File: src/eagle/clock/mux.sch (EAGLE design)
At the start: 53 parts, among them U1 SN74HC595N, U2 SN74HC595N, U3 SN74HC595N

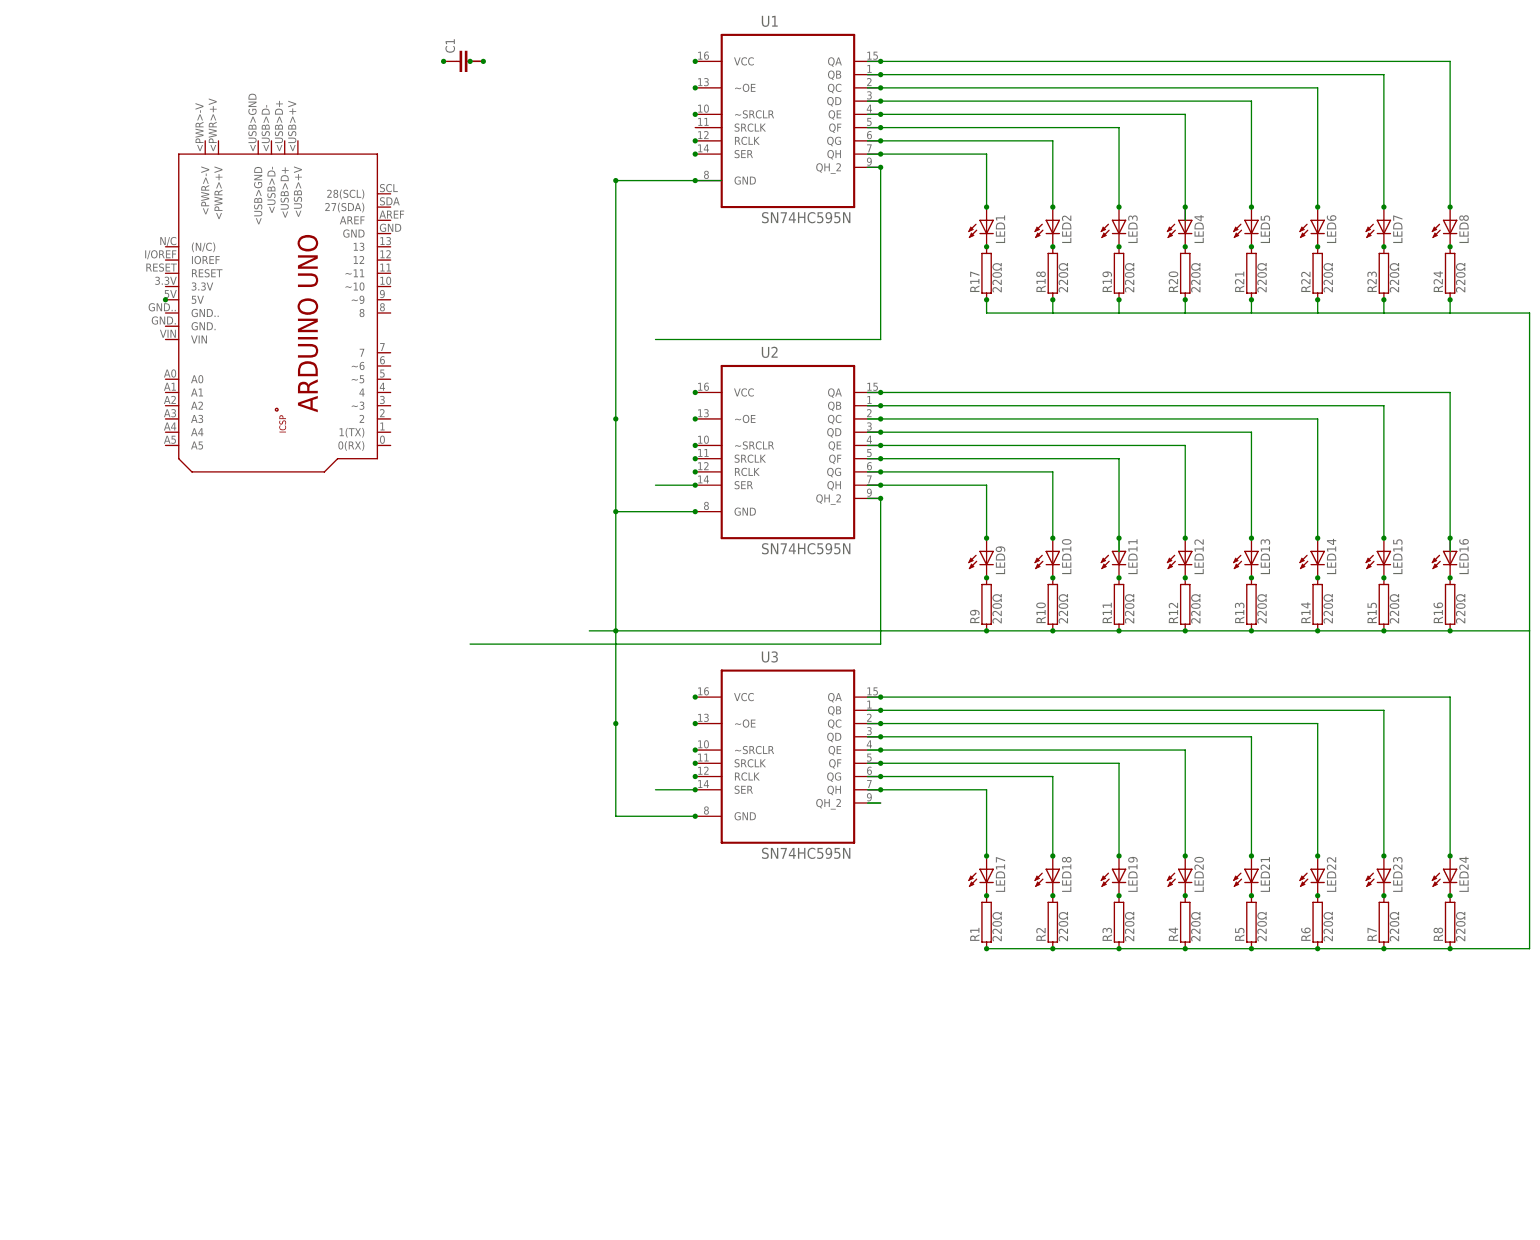
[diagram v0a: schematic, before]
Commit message: Add another mux. Add labels to all LEDs
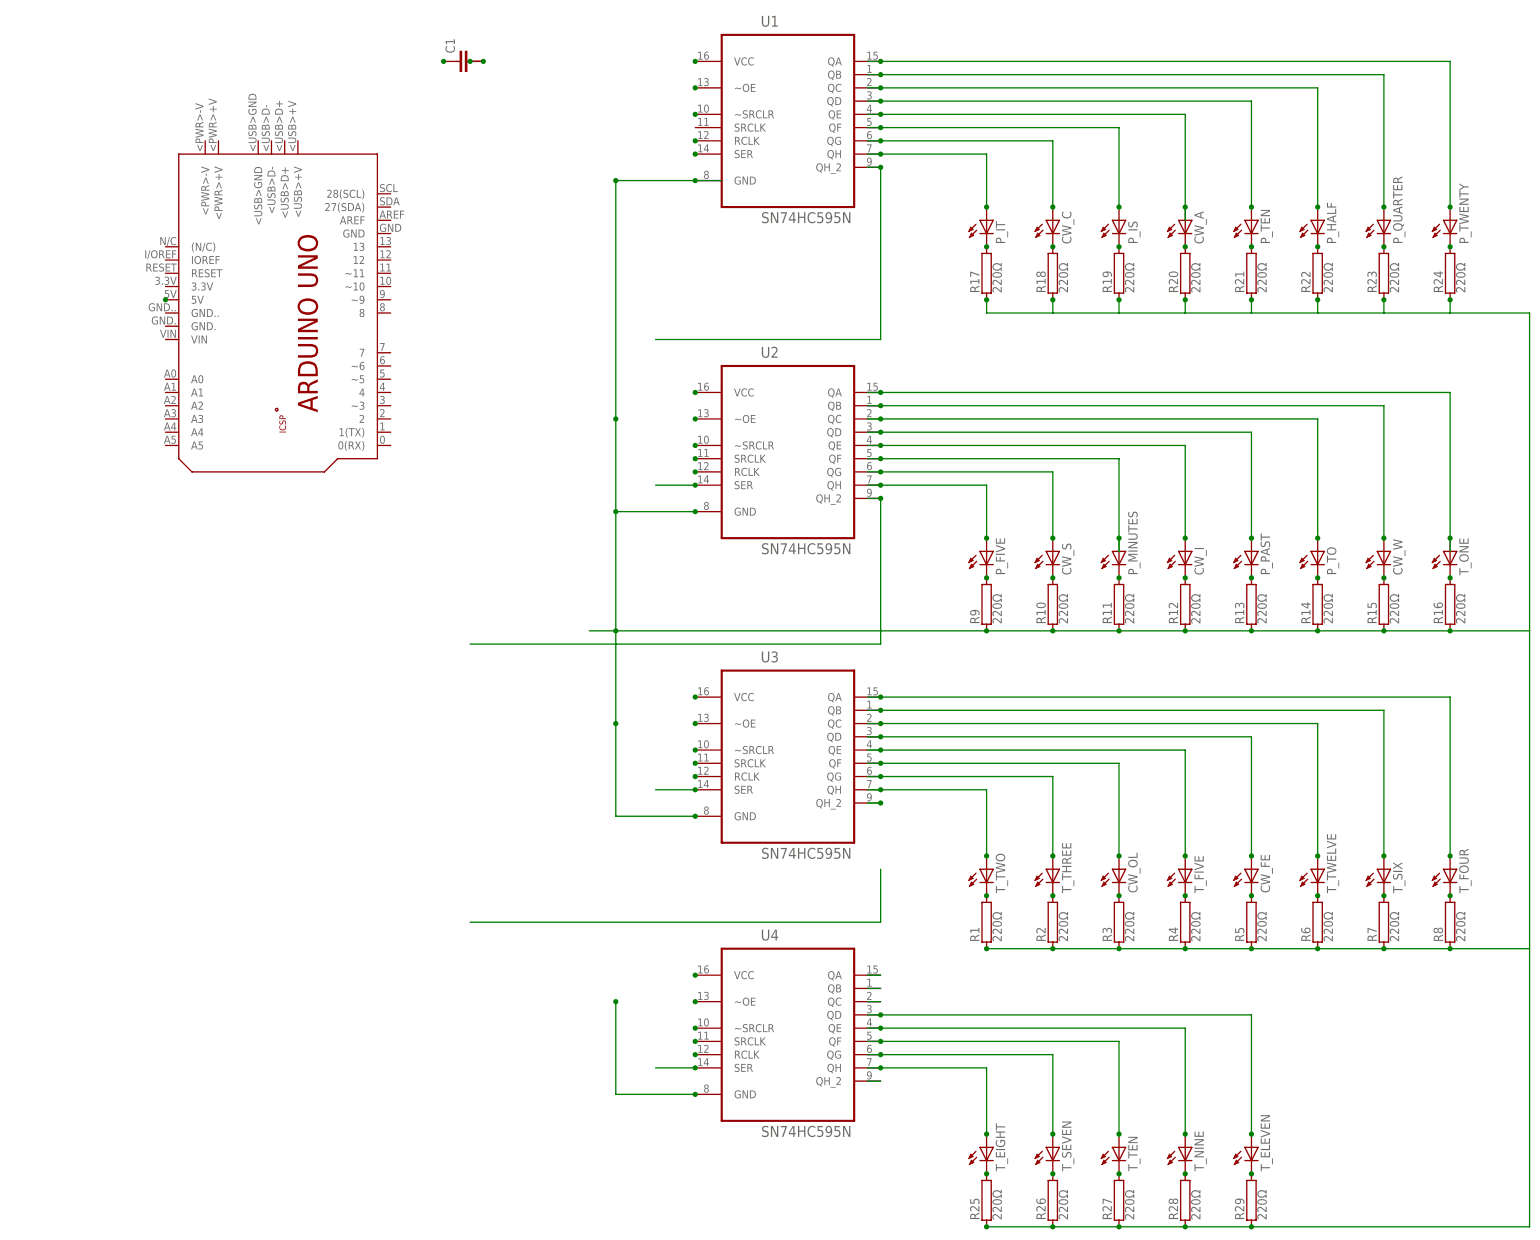
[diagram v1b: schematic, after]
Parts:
- added R25, R26, R27, R28, R29: 220Ω, resistor-power:RCA4050
- added T_EIGHT, T_ELEVEN, T_NINE, T_SEVEN, T_TEN: (no value), led:LEDSMT1206
- added U4: SN74HC595N, SN74HC595N:SN74HC595N
- renumbered LED1 to P_IT, LED10 to CW_S, LED11 to P_MINUTES, LED12 to CW_I, LED13 to P_PAST, LED14 to P_TO, LED15 to CW_W, LED16 to T_ONE, LED17 to T_TWO, LED18 to T_THREE, LED19 to CW_OL, LED2 to CW_C, LED20 to T_FIVE, LED21 to CW_FE, LED22 to T_TWELVE, LED23 to T_SIX, LED24 to T_FOUR, LED3 to P_IS, LED4 to CW_A, LED5 to P_TEN, LED6 to P_HALF, LED7 to P_QUARTER, LED8 to P_TWENTY, LED9 to P_FIVE
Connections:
- net N$18 renamed CW_C
- net N$30 renamed CW_W
- net N$6 renamed T_TWELVE
- removed net N$26: R1.1, R10.1, R11.1, R12.1, R13.1, R14.1, R15.1, R16.1, R17.1, R18.1, R19.1, R2.1, R20.1, R21.1, R22.1, R23.1, R24.1, R3.1, R4.1, R5.1, R6.1, R7.1, R8.1, R9.1, U1.GND, U2.GND, U3.GND
- new net N$18: R25.2, T_EIGHT.C
- new net N$73: R26.2, T_SEVEN.C
- new net N$74: R27.2, T_TEN.C
- new net N$75: R28.2, T_NINE.C
- new net N$76: R29.2, T_ELEVEN.C
- new net N$80: R1.1, R10.1, R11.1, R12.1, R13.1, R14.1, R15.1, R16.1, R17.1, R18.1, R19.1, R2.1, R20.1, R21.1, R22.1, R23.1, R24.1, R25.1, R26.1, R27.1, R28.1, R29.1, R3.1, R4.1, R5.1, R6.1, R7.1, R8.1, R9.1, U1.GND, U2.GND, U3.GND, U4.GND
- new net N$81: T_SEVEN.A, U4.QG
- new net N$82: T_TEN.A, U4.QF
- new net N$83: T_ELEVEN.A, U4.QD
- new net N$84: U4.QC
- new net N$85: U4.QB
- new net N$86: U4.QA
- new net N$87: T_NINE.A, U4.QE
- new net N$88: T_EIGHT.A, U4.QH
- new net N$90: U4.QH_2
- new net N$91: U4.VCC
- new net N$92: U4.~OE
- new net N$93: U4.~SRCLR
- new net N$94: U4.SER
- new net N$95: U4.SRCLK
- new net N$96: U4.RCLK

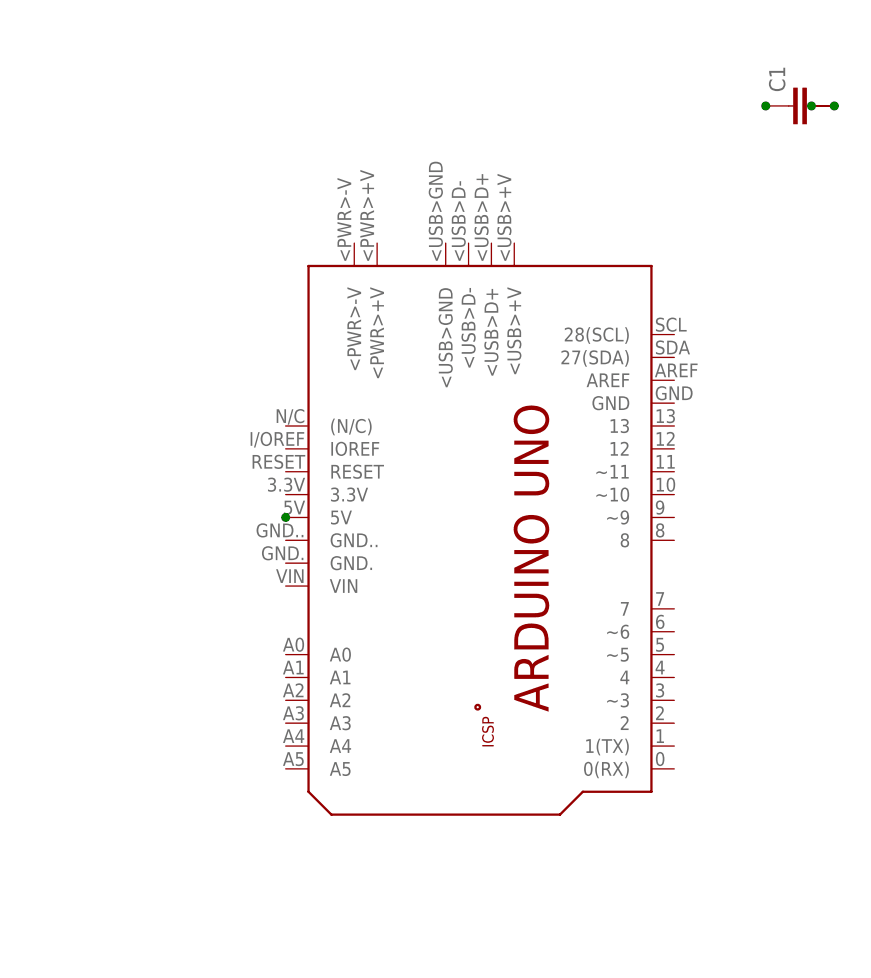
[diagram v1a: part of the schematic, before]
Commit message: move arduino left
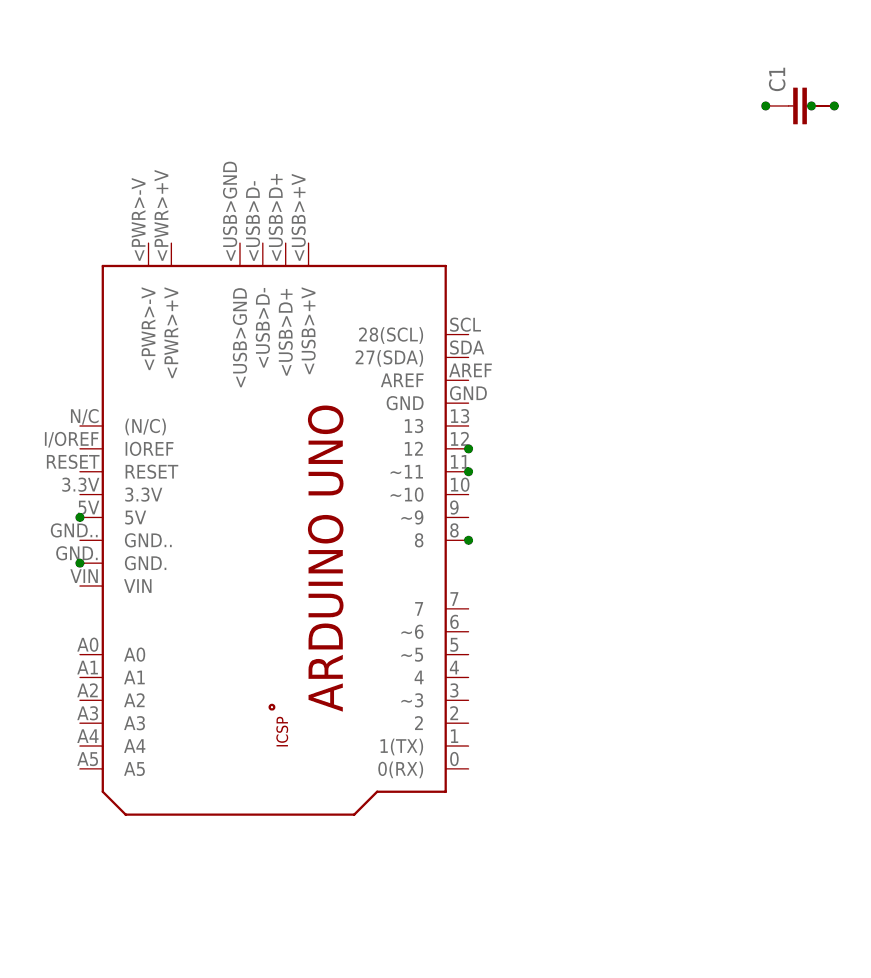
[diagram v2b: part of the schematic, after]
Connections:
- new net N$26: PCB1.8
- new net N$30: PCB1.~11
- new net N$6: PCB1.GND.
- new net N$77: PCB1.12
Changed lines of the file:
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@@
 <wire x1="0" y1="-48.26" x2="-116.84" y2="-48.26" width="0.1524" layer="93"/>
 <wire x1="-116.84" y1="-48.26" x2="-116.84" y2="10.16" width="0.1524" layer="93"/>
-<wire x1="-116.84" y1="10.16" x2="-81.28" y2="10.16" width="0.1524" layer="93"/>
+<wire x1="-116.84" y1="10.16" x2="-104.14" y2="10.16" width="0.1524" layer="93"/>
 <wire x1="-7.62" y1="-2.54" x2="-7.62" y2="-10.16" width="0.1524" layer="93"/>
 <wire x1="-7.62" y1="-10.16" x2="-7.62" y2="-60.96" width="0.1524" layer="93"/>
 <wire x1="-7.62" y1="-60.96" x2="-7.62" y2="-71.12" width="0.1524" layer="93"/>
 <wire x1="-116.84" y1="60.96" x2="-116.84" y2="15.24" width="0.1524" layer="93"/>
-<wire x1="-116.84" y1="15.24" x2="-81.28" y2="15.24" width="0.1524" layer="93"/>
+<wire x1="-116.84" y1="15.24" x2="-101.6" y2="15.24" width="0.1524" layer="93"/>
 <wire x1="-116.84" y1="60.96" x2="-7.62" y2="60.96" width="0.1524" layer="93"/>
 <wire x1="20.32" y1="55.88" x2="5.08" y2="55.88" width="0.1524" layer="93"/>
@@
 <wire x1="-7.62" y1="-60.96" x2="2.54" y2="-60.96" width="0.1524" layer="93"/>
 <wire x1="7.62" y1="-60.96" x2="20.32" y2="-60.96" width="0.1524" layer="93"/>
-<wire x1="-38.1" y1="20.32" x2="-22.86" y2="20.32" width="0.1524" layer="93"/>
+<wire x1="-60.96" y1="20.32" x2="-22.86" y2="20.32" width="0.1524" layer="93"/>
 <wire x1="-22.86" y1="20.32" x2="-22.86" y2="43.18" width="0.1524" layer="93"/>
 <wire x1="-22.86" y1="43.18" x2="-10.16" y2="43.18" width="0.1524" layer="93"/>
@@
 <wire x1="2.54" y1="-78.74" x2="7.62" y2="-78.74" width="0.1524" layer="93" curve="-180"/>
 <wire x1="2.54" y1="-71.12" x2="7.62" y2="-71.12" width="0.1524" layer="93" curve="-180"/>
-<wire x1="-38.1" y1="22.86" x2="-25.4" y2="22.86" width="0.1524" layer="93"/>
+<wire x1="-60.96" y1="22.86" x2="-25.4" y2="22.86" width="0.1524" layer="93"/>
 <wire x1="-25.4" y1="17.78" x2="-25.4" y2="-10.16" width="0.1524" layer="93"/>
 <wire x1="-25.4" y1="-10.16" x2="-25.4" y2="-45.72" width="0.1524" layer="93"/>
@@
 <wire x1="-25.4" y1="-68.58" x2="-20.32" y2="-68.58" width="0.1524" layer="93" curve="-180"/>
 <wire x1="-22.86" y1="-7.62" x2="-22.86" y2="-12.7" width="0.1524" layer="93" curve="-180"/>
-<wire x1="-38.1" y1="12.7" x2="-27.94" y2="12.7" width="0.1524" layer="93"/>
+<wire x1="-60.96" y1="12.7" x2="-27.94" y2="12.7" width="0.1524" layer="93"/>
 <wire x1="-27.94" y1="12.7" x2="-27.94" y2="-17.78" width="0.1524" layer="93"/>
 <wire x1="-20.32" y1="-17.78" x2="-10.16" y2="-17.78" width="0.1524" layer="93"/>
@@
 <instance part="U2" gate="A" x="38.1" y="-10.16"/>
 <instance part="U3" gate="A" x="38.1" y="-68.58"/>
-<instance part="PCB1" gate="G$1" x="-58.42" y="12.7" rot="R270"/>
+<instance part="PCB1" gate="G$1" x="-81.28" y="12.7" rot="R270"/>
 <instance part="C1" gate="G$1" x="-25.4" y="60.96" rot="R90"/>
 <instance part="T_EIGHT" gate="G$1" x="76.2" y="-147.32"/>
@@
 <segment>
 <pinref part="PCB1" gate="G$1" pin="5V"/>
-<junction x="-81.28" y="15.24"/>
+<junction x="-104.14" y="15.24"/>
 </segment>
 </net>
@@
 </segment>
 </net>
+<net name="N$6" class="0">
+<segment>
+<pinref part="PCB1" gate="G$1" pin="GND."/>
+<junction x="-104.14" y="10.16"/>
+</segment>
+</net>
+<net name="N$26" class="0">
+<segment>
+<pinref part="PCB1" gate="G$1" pin="8"/>
+<junction x="-60.96" y="12.7"/>
+</segment>
+</net>
+<net name="N$30" class="0">
+<segment>
+<pinref part="PCB1" gate="G$1" pin="~11"/>
+<junction x="-60.96" y="20.32"/>
+</segment>
+</net>
+<net name="N$77" class="0">
+<segment>
+<pinref part="PCB1" gate="G$1" pin="12"/>
+<junction x="-60.96" y="22.86"/>
+</segment>
+</net>
